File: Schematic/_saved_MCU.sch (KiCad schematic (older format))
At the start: 6 parts, among them U1 STM32F427VGTx, U2 AH1806-W, U3 FT232RL

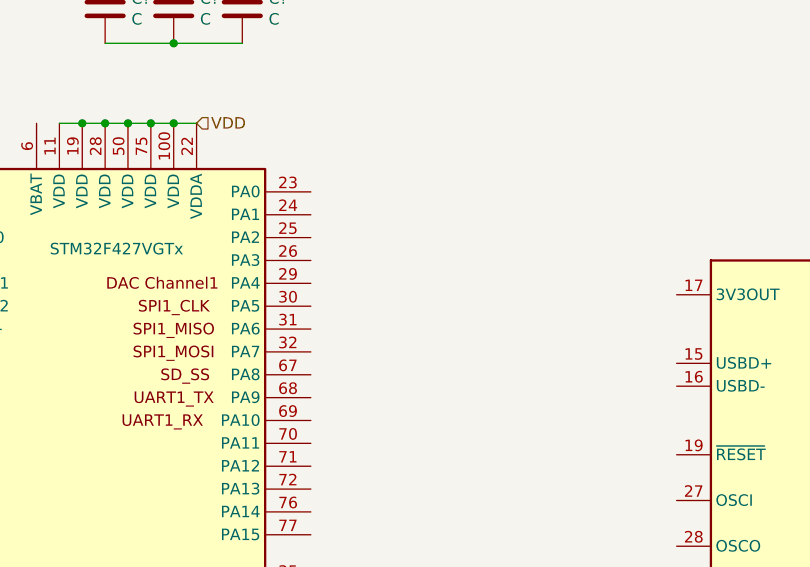
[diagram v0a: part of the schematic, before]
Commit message: Add power circuitry
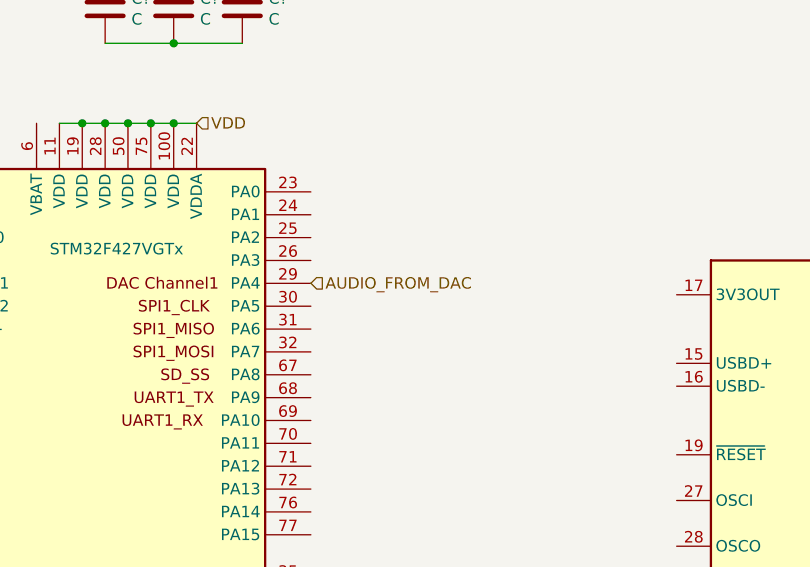
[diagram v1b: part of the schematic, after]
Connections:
- net AUDIO_FROM_DAC: now reaches U1.29 (PA4)
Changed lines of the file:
@@
 	2900 1050 3200 1050
 Connection ~ 2900 1050
+Text HLabel 3500 2100 2    50   Input ~ 0
+AUDIO_FROM_DAC
 $EndSCHEMATC
